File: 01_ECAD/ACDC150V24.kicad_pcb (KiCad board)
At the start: 2 copper layers, 85 x 120 mm, 72 parts, among them J1 B2P3-VH(LF)(SN), J2 B4P-VH(LF)(SN), Q1 IXFH20N100P, SW1 NE18 2A EE 6AMP, U1 UCC28600, U2 CNY17-1, U3 TL431DBZ

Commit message: Update.
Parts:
- added C28: 1nF, Capacitor_THT:C_Disc_D7.5mm_W5.0mm_P7.50mm, F.Cu at (74.3, 122.1)
- added HS2: V5629W220, PS:V5629W220, F.Cu at (84.5, 118.1)
- added R19: 4.3k, Resistor_SMD:R_0603_1608Metric, F.Cu at (114.4, 112.9)
- added R20: 47, Resistor_THT:R_Axial_DIN0516_L15.5mm_D5.0mm_P5.08mm_Vertical, F.Cu at (74.3, 126.1)
- D1: value RB520SM-40T2R -> PMEG100T10ELXDX; footprint Diode_SMD:D_SOD-523 -> Diode_SMD:D_SOD-323
- D2, D3: value VS-2EMH01HM3/5AT -> PMEG100T10ELXDX; footprint Diode_SMD:D_SMA -> Diode_SMD:D_SOD-323
- R15: value 35.2k -> 4.3k
- R16: value 4.12k -> 1k
- R17, R18: footprint Resistor_SMD:R_2512_6332Metric -> Resistor_THT:R_Axial_DIN0516_L15.5mm_D5.0mm_P5.08mm_Vertical
- R8: footprint Resistor_SMD:R_1206_3216Metric_Pad1.30x1.75mm_HandSolder -> Resistor_SMD:R_0603_1608Metric
- moved C19 50.8 mm to (99.7, 129.2), turned to 180 degrees
- moved C22 50.6 mm to (105.8, 124.0), turned to 0 degrees
- moved C23 43.6 mm to (65.9, 133.3), turned to -90 degrees
- moved C24 34.9 mm to (52.5, 133.3), turned to -90 degrees
- moved R8 20.2 mm to (65.9, 80.9), turned to -90 degrees
- moved C16 18.2 mm to (99.7, 125.1), turned to 0 degrees
- moved D2 15.6 mm to (67.7, 80.8), turned to -90 degrees
- moved C21 7.63 mm to (81.8, 135.8), turned to 180 degrees
- moved C26 4.96 mm to (91.8, 115.0), turned to 180 degrees
- moved D7 4.13 mm to (78.7, 115.6)
- moved C18 4.05 mm to (99.7, 131.3), turned to 0 degrees
- moved C17 3.80 mm to (99.7, 127.2), turned to 180 degrees
- moved L1 3.78 mm to (92.1, 127.2), turned to 180 degrees
- moved R13 3.38 mm to (110.6, 110.6), turned to 90 degrees
- moved C25 1.87 mm to (91.8, 117.0), turned to 0 degrees
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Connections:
- C3 pad 1: Net-(D2-K) -> Net-(U1-VDD)
- C4 pad 1: Net-(D2-K) -> Net-(U1-VDD)
- C5 pad 1: Net-(D2-K) -> Net-(U1-VDD)
- C6 pad 1: Net-(D3-K) -> Net-(D2-A)
- D3 pad 1: Net-(D3-K) -> Net-(D2-A)
- R14 pad 2: /PS/24V_O -> /PS/24V_F
- R15 pad 1: Net-(U3-REF) -> Net-(R15-Pad1)
- R15 pad 2: /PS/24V_O -> /PS/24V_F
- R7 pad 1: Net-(D2-K) -> Net-(U1-VDD)
- R8 pad 1: Net-(D3-K) -> Net-(D2-K)
- R8 pad 2: Net-(D2-A) -> Net-(U1-VDD)
- U1 pad 6: Net-(D2-K) -> Net-(U1-VDD)
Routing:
- net OUT_GND: track 73.4 -> 17.8 mm, vias 2 -> 5
- net Net-(D2-A): track 2.85 -> 44.7 mm, vias 0 -> 1
- net Net-(D3-K): track 37.3 -> 0.00 mm, vias 1 -> 0
- net Net-(D2-K): track 34.5 -> 1.87 mm
- net Net-(U1-VDD): track 0.00 -> 23.8 mm
- net GND_DC_P: track 49.5 -> 28.9 mm, vias 7 -> 20
- net /PS/24V_O: track 14.1 -> 0.00 mm
- net Net-(U3-REF): track 18.0 -> 12.4 mm
- net Net-(C28-Pad1): track 0.00 -> 4.07 mm
- net Net-(U3-K): track 14.8 -> 11.7 mm
- net Net-(C20-Pad2): track 4.31 -> 6.25 mm
- net Net-(D6-K): track 12.3 -> 13.8 mm
- net Net-(R15-Pad1): track 0.00 -> 1.32 mm
- net Net-(C14-Pad1): track 1.52 -> 2.54 mm
- net /PS/24V_F: track 8.21 -> 9.12 mm
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- added copper zone on B.Cu, net Net-(D7A-A)
- removed copper zone on B.Cu, net /PS/24V_F
- removed copper zone on B.Cu, net /PS/24V_O
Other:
- board text added: "+"
- board text removed: "+24V GND"

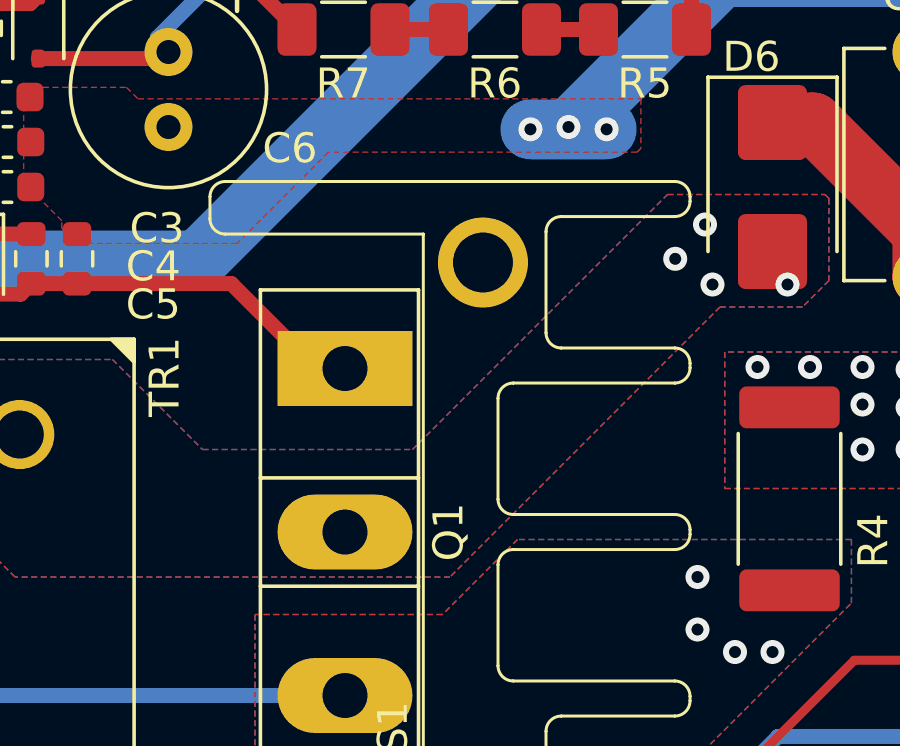
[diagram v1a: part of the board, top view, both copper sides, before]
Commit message: Adding To-Do.txt , First initial working Design.
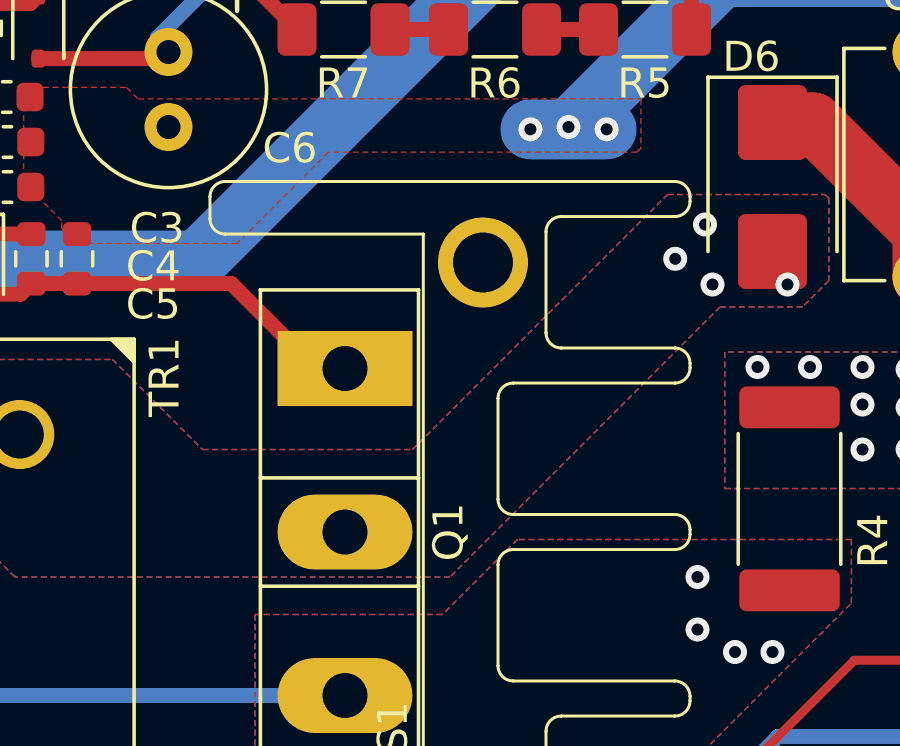
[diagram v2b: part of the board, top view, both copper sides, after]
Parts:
- C13: value 43pF -> 68pF
- C14: value 27nF -> 56nF
- R11: value 1K -> 499
- R13: value 93.1k -> 48.7K
- R15: value 4.3k -> 36K
- R16: value 1k -> 4.3K
- R19: value 4.3k -> 976
